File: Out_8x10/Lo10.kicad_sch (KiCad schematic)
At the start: 32 parts, among them J7 Conn_01x09, J8 Conn_01x12, Q17 AO3400A, Q18 AO3400A, Q19 AO3400A, Q20 AO3400A, Q21 AO3400A, Q22 AO3400A, Q23 AO3400A, Q24 AO3400A, Q25 AO3400A, Q26 AO3400A

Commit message: updated layout
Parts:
- J8: footprint Connector_Molex:Molex_KK-396_5273-10A_1x10_P3.96mm_Vertical -> Connector_Molex:Molex_KK-396_5273-12A_1x12_P3.96mm_Vertical
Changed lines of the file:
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@@
       (effects (font (size 1.27 1.27)) (justify left))
     )
-    (property "Footprint" "Connector_Molex:Molex_KK-396_5273-10A_1x10_P3.96mm_Vertical" (id 2) (at 238.76 124.46 0)
+    (property "Footprint" "Connector_Molex:Molex_KK-396_5273-12A_1x12_P3.96mm_Vertical" (id 2) (at 238.76 124.46 0)
       (effects (font (size 1.27 1.27)) hide)
     )

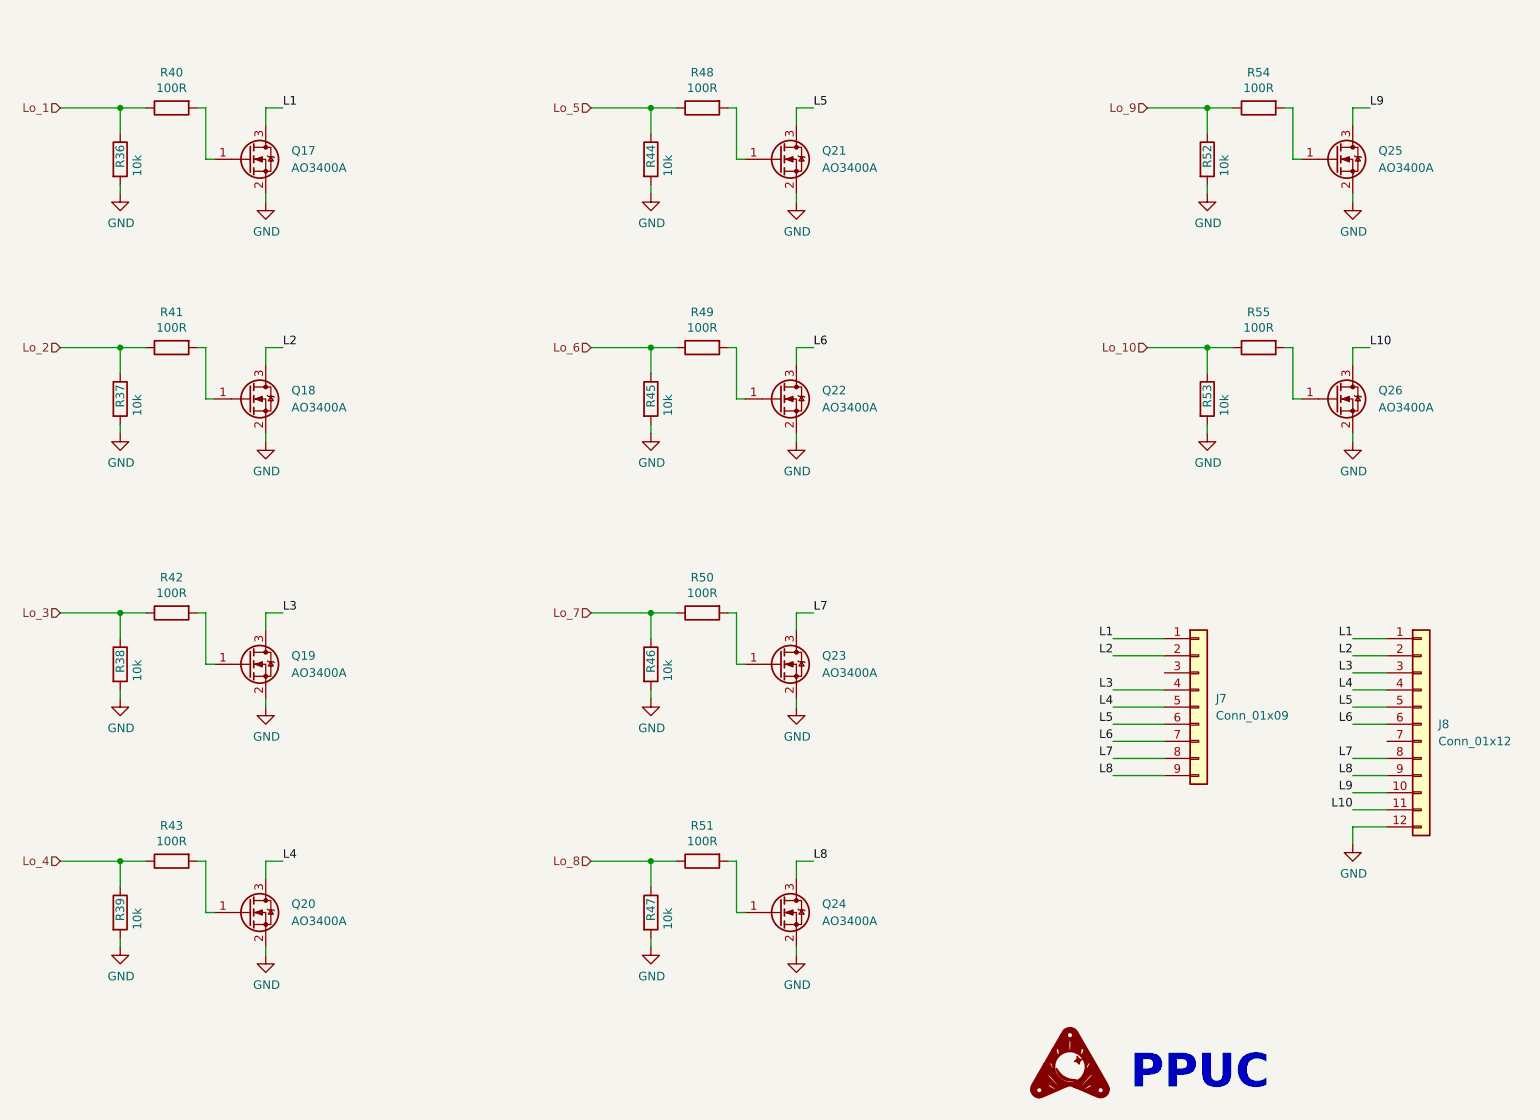
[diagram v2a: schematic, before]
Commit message: updated layout
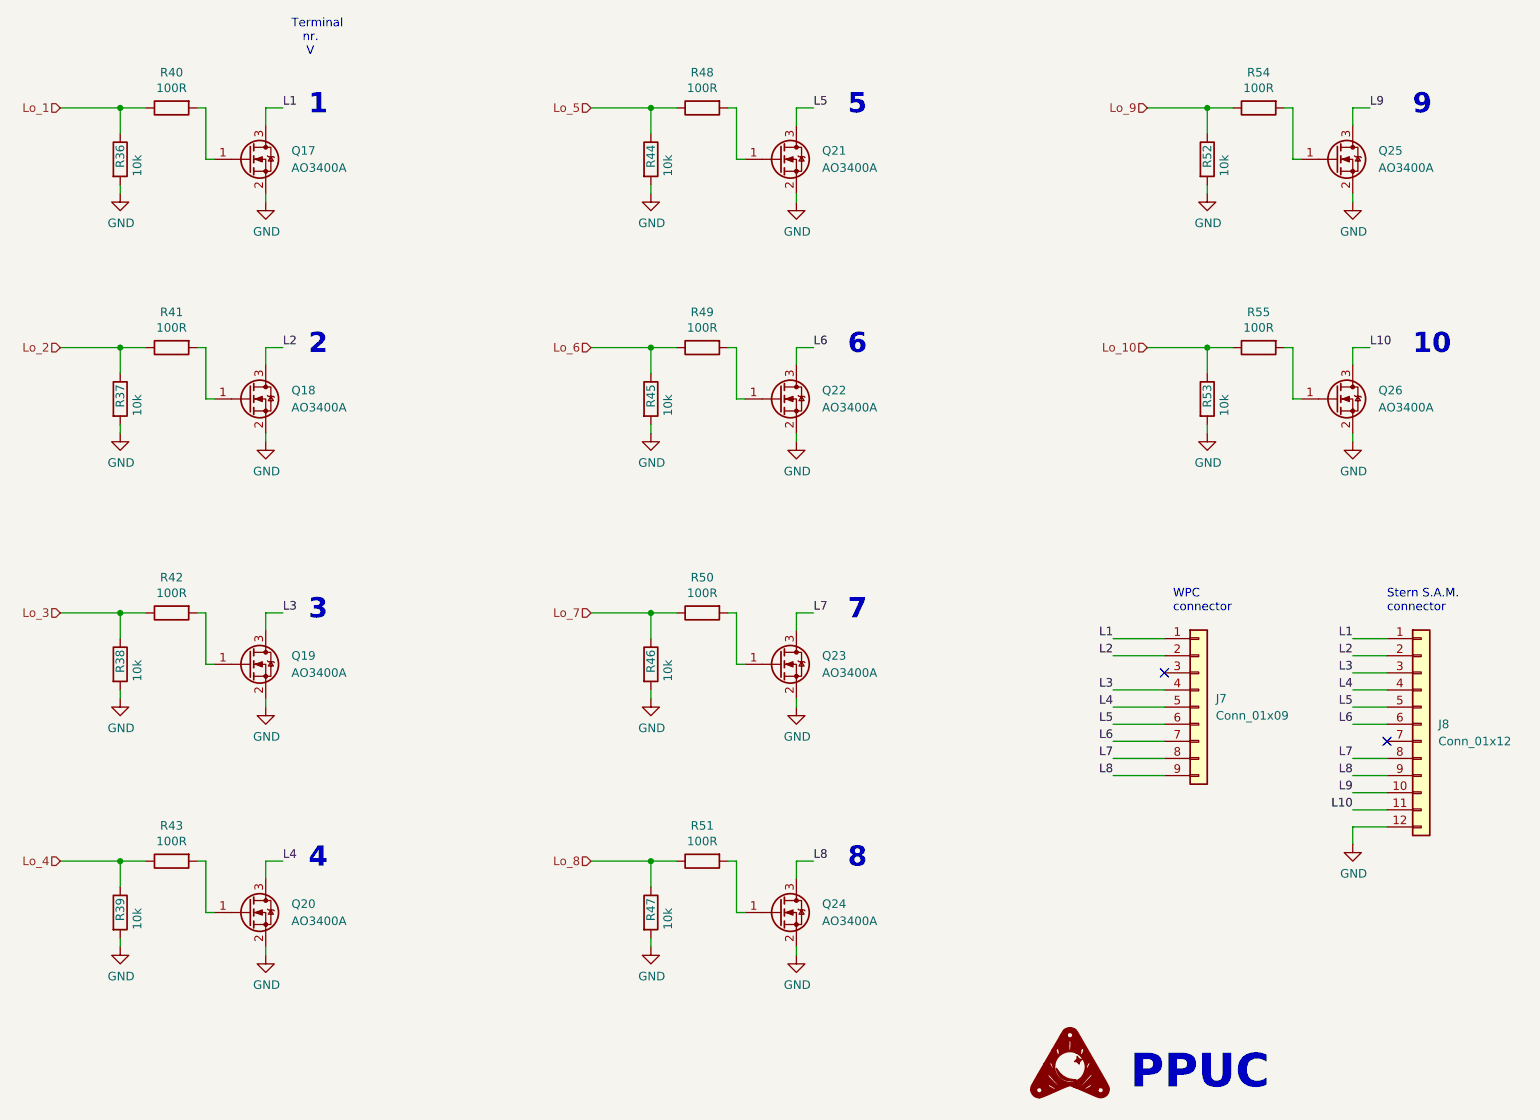
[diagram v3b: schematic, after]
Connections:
- no-connect marks 0 -> 2
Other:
- note added: "1"
- note added: "10"
- note added: "2"
- note added: "3"
- note added: "4"
- note added: "5"
- note added: "6"
- note added: "7"
- note added: "8"
- note added: "9"
- note added: "Stern S.A.M. connector"
- note added: "Terminal nr. V"
- note added: "WPC connector"
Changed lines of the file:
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@@
   (junction (at 45.72 107.95) (diameter 0) (color 0 0 0 0)
   )
+  (no_connect (at 233.68 127))
+  (no_connect (at 200.66 116.84))
   (wire (pts (xy 193.04 132.08) (xy 200.66 132.08))
     (stroke (width 0) (type default) (color 0 0 0 0))
@@
   (wire (pts (xy 228.6 45.72) (xy 228.6 46.99))
     (stroke (width 0) (type default) (color 0 0 0 0))
+  )
+  (text "9" (at 237.49 34.29 0)
+    (effects (font (size 3 3) (thickness 0.6) bold) (justify left bottom))
+  )
+  (text "8" (at 153.67 146.05 0)
+    (effects (font (size 3 3) (thickness 0.6) bold) (justify left bottom))
+  )
+  (text "10" (at 237.49 69.85 0)
+    (effects (font (size 3 3) (thickness 0.6) bold) (justify left bottom))
+  )
+  (text "5" (at 153.67 34.29 0)
+    (effects (font (size 3 3) (thickness 0.6) bold) (justify left bottom))
+  )
+  (text "6" (at 153.67 69.85 0)
+    (effects (font (size 3 3) (thickness 0.6) bold) (justify left bottom))
+  )
+  (text "1" (at 73.66 34.29 0)
+    (effects (font (size 3 3) (thickness 0.6) bold) (justify left bottom))
+  )
+  (text "7" (at 153.67 109.22 0)
+    (effects (font (size 3 3) (thickness 0.6) bold) (justify left bottom))
+  )
+  (text "4" (at 73.66 146.05 0)
+    (effects (font (size 3 3) (thickness 0.6) bold) (justify left bottom))
   )
   (text "PPUC" (at 195.58 179.07 0)
     (effects (font (size 5 5) bold) (justify left bottom))
   )
+  (text "WPC\nconnector\n" (at 201.93 107.95 0)
+    (effects (font (size 1.27 1.27)) (justify left bottom))
+  )
+  (text "3" (at 73.66 109.22 0)
+    (effects (font (size 3 3) (thickness 0.6) bold) (justify left bottom))
+  )
+  (text "Terminal\n   nr.\n    V" (at 71.12 25.4 0)
+    (effects (font (size 1.27 1.27)) (justify left bottom))
+  )
+  (text "Stern S.A.M.\nconnector\n" (at 233.68 107.95 0)
+    (effects (font (size 1.27 1.27)) (justify left bottom))
+  )
+  (text "2" (at 73.66 69.85 0)
+    (effects (font (size 3 3) (thickness 0.6) bold) (justify left bottom))
+  )
   (label "L2" (at 228.6 114.3 180)
